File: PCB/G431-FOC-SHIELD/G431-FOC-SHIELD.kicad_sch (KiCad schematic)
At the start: 34 parts, among them CN10 Conn_02x19_Odd_Even, CN7 Conn_02x19_Odd_Even, J1 Screw_Terminal_01x02, J2 Screw_Terminal_01x03, Q1 Q_NMOS_GDS, Q2 Q_NMOS_GDS, Q3 Q_NMOS_GDS, Q4 Q_NMOS_GDS, Q5 Q_NMOS_GDS, Q6 Q_NMOS_GDS, U1 DRV8323RSRGZR

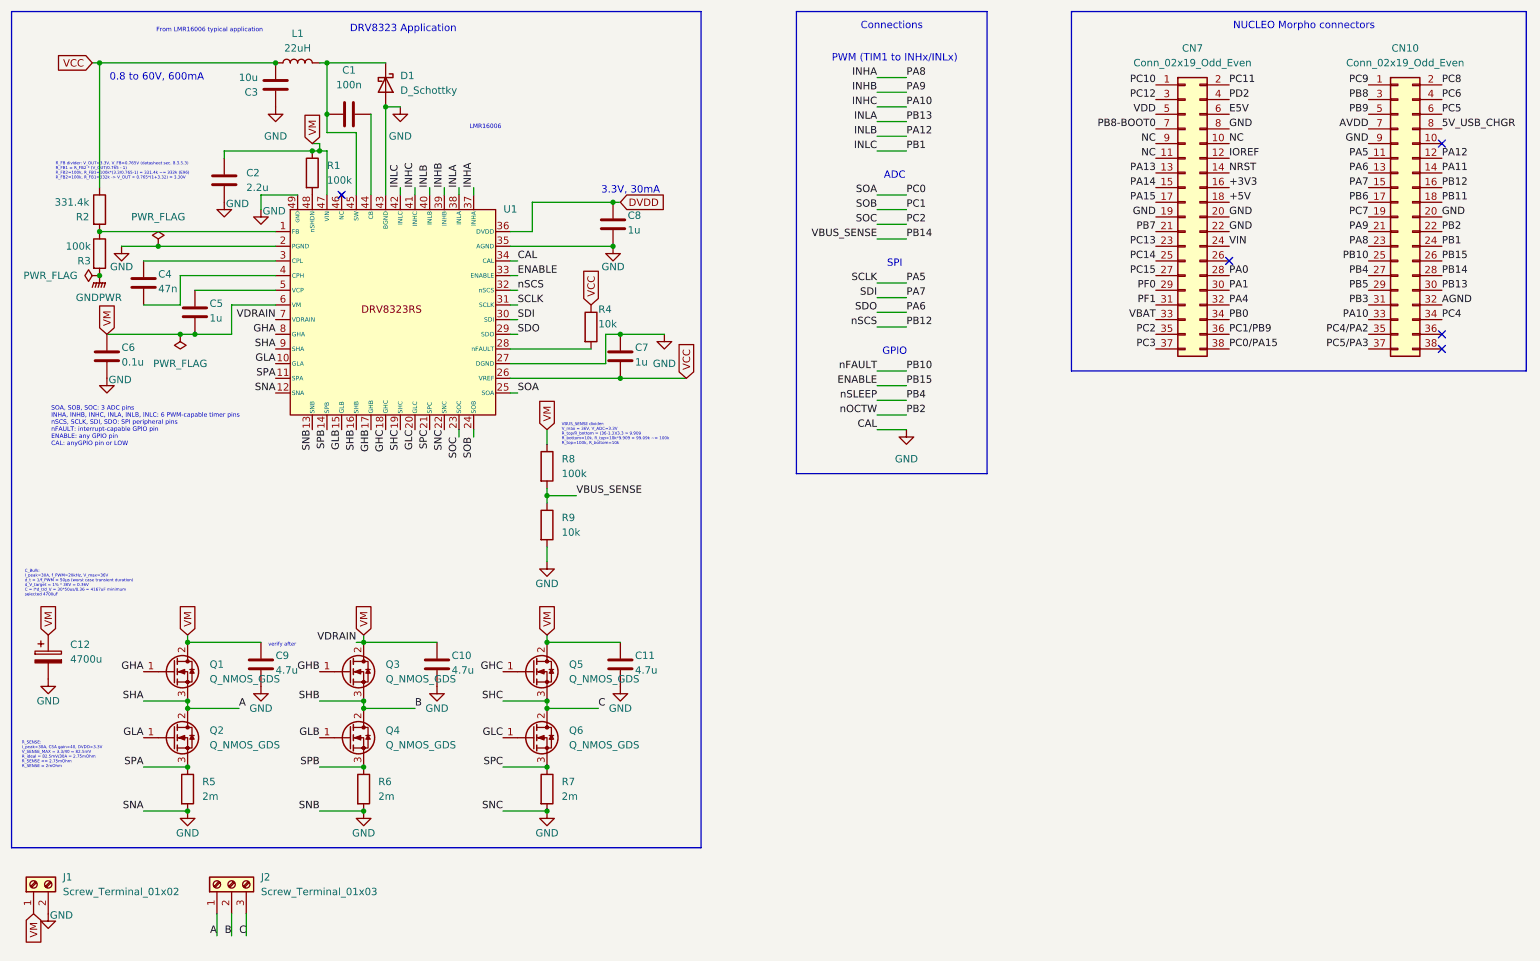
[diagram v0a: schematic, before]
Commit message: using custom cad for edge, placement started
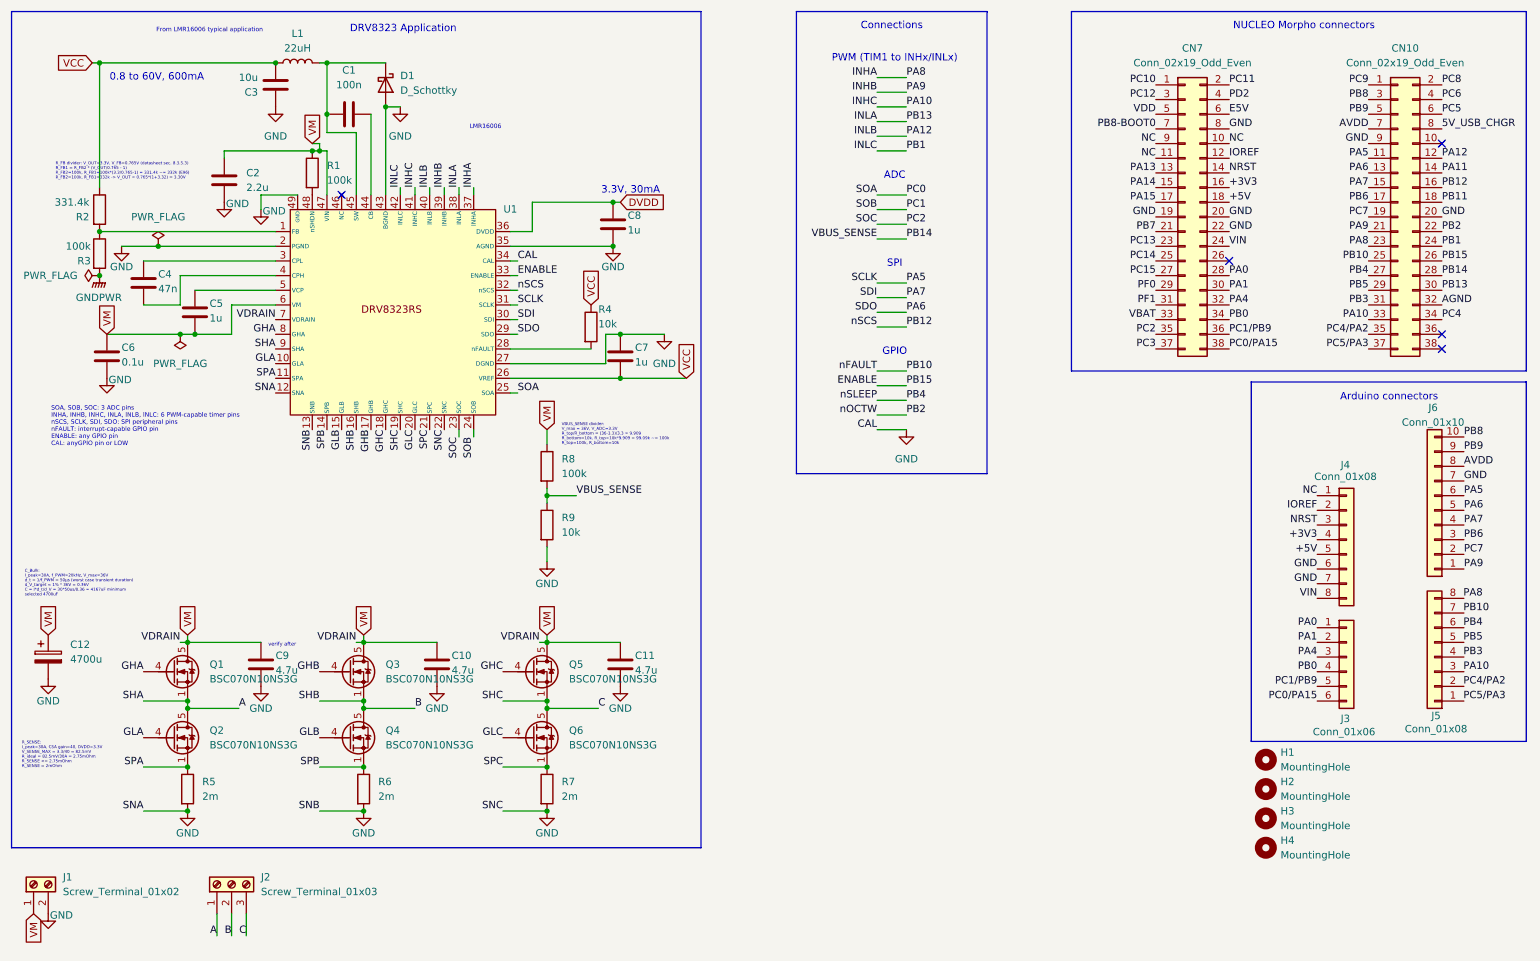
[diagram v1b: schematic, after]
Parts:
- removed Q1, Q2, Q3, Q4, Q5, Q6: Q_NMOS_GDS, Package_TO_SOT_SMD:TO-263-3_TabPin2, symbol Transistor_FET:Q_NMOS_GDS
- added H1, H2, H3, H4: MountingHole, MountingHole:MountingHole_3.2mm_M3, symbol Mechanical:MountingHole
- added J3: Conn_01x06, Connector_PinHeader_2.54mm:PinHeader_1x06_P2.54mm_Vertical, symbol Connector_Generic:Conn_01x06
- added J4, J5: Conn_01x08, Connector_PinHeader_2.54mm:PinHeader_1x08_P2.54mm_Vertical, symbol Connector_Generic:Conn_01x08
- added J6: Conn_01x10, Connector_PinHeader_2.54mm:PinHeader_1x10_P2.54mm_Vertical, symbol Connector_Generic:Conn_01x10
- added Q1, Q2, Q3, Q4, Q5, Q6: BSC070N10NS3G, Package_TO_SOT_SMD:TDSON-8-1, symbol Transistor_FET:BSC070N10NS3G
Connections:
- net +3V3: now also J4.4 (Pin_4)
- net +5V: now also J4.5 (Pin_5)
- net A: now also Q1.1 (S), Q1.2 (S), Q1.3 (S), Q2.5 (D)
- net AVDD: now also J6.8 (Pin_8)
- net B: now also Q3.1 (S), Q3.2 (S), Q3.3 (S), Q4.5 (D)
- net C: now also Q5.1 (S), Q5.2 (S), Q5.3 (S), Q6.5 (D)
- net GHA: now also Q1.4 (G)
- net GHB: now also Q3.4 (G)
- net GHC: now also Q5.4 (G)
- net GLA: now also Q2.4 (G)
- net GLB: now also Q4.4 (G)
- net GLC: now also Q6.4 (G)
- net GND: now also J4.6 (Pin_6), J4.7 (Pin_7), J6.7 (Pin_7)
- net INHB: now also J6.1 (Pin_1)
- net IOREF: now also J4.2 (Pin_2)
- net NC: now also J4.1 (Pin_1)
- net NRST: now also J4.3 (Pin_3)
- net PA0: now also J3.1 (Pin_1)
- net PA1: now also J3.2 (Pin_2)
- net PA4: now also J3.3 (Pin_3)
- net PA5: now also J6.6 (Pin_6)
- net PA6: now also J6.5 (Pin_5)
- net PA7: now also J6.4 (Pin_4)
- net PB0: now also J3.4 (Pin_4)
- net PB6: now also J6.3 (Pin_3)
- net PB8: now also J6.10 (Pin_10)
- net PB9: now also J6.9 (Pin_9)
- net PC0/PA15: now also J3.6 (Pin_6)
- net PC1/PB9: now also J3.5 (Pin_5)
- net PC7: now also J6.2 (Pin_2)
- net SPA: now also Q2.1 (S), Q2.2 (S), Q2.3 (S)
- net SPB: now also Q4.1 (S), Q4.2 (S), Q4.3 (S)
- net SPC: now also Q6.1 (S), Q6.2 (S), Q6.3 (S)
- net VIN: now also J4.8 (Pin_8)
- net VM: now also Q1.5 (D), Q3.5 (D), Q5.5 (D)
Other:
- note added: "Arduino connectors"

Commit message: routed motor drive stuff, started header pin routing
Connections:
- net PC0 is gone; now on net PC0/PA15: U1.25 (SOA)
- net PC1 is gone; now on net PC1/PB9: U1.24 (SOB)
- net +3V3: no longer J4.4 (Pin_4)
- net +5V: no longer J4.5 (Pin_5)
- net AVDD: no longer J6.8 (Pin_8)
- net GND: no longer J4.6 (Pin_6), J4.7 (Pin_7), J6.7 (Pin_7)
- net INHB: no longer J6.1 (Pin_1)
- net IOREF: no longer J4.2 (Pin_2)
- net NC: no longer J4.1 (Pin_1)
- net NRST: no longer J4.3 (Pin_3)
- net PA0: no longer J3.1 (Pin_1)
- net PA1: no longer J3.2 (Pin_2)
- net PA4: no longer J3.3 (Pin_3)
- net PA5: no longer J6.6 (Pin_6)
- net PA6: no longer J6.5 (Pin_5)
- net PA7: no longer J6.4 (Pin_4)
- net PB0: no longer J3.4 (Pin_4)
- net PB6: no longer J6.3 (Pin_3)
- net PB8: no longer J6.10 (Pin_10)
- net PB9: no longer J6.9 (Pin_9)
- net PC0/PA15: no longer J3.6 (Pin_6)
- net PC1/PB9: no longer J3.5 (Pin_5)
- net PC7: no longer J6.2 (Pin_2)
- net VIN: no longer J4.8 (Pin_8)
- no-connect marks 5 -> 37
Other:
- note added: "Net Classes"
